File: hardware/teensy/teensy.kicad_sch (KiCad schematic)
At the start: 1 part, among them U1 Teensy3.5

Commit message: still learning kicad
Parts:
- added J1: CONN_16, Connectors:1X16, symbol SparkFun-Connectors:CONN_16
- added R1: 33OHM-0603-1_10W-1%, Resistors:AXIAL-0.3, symbol SparkFun-Resistors:33OHM-0603-1_10W-1%
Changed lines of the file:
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@@
     (stroke (width 0) (type solid) (color 0 0 0 0))
+  )
+  (symbol (lib_id "SparkFun-Resistors:33OHM-0603-1_10W-1%") (at 111.76 39.37 0) (unit 1)
+    (in_bom yes) (on_board yes)
+    (property "Reference" "R1" (id 0) (at 111.76 30.48 0)
+      (effects (font (size 1.143 1.143)))
+    )
+    (property "Value" "33OHM-0603-1_10W-1%" (id 1) (at 111.76 33.02 0)
+      (effects (font (size 1.143 1.143)))
+    )
+    (property "Footprint" "Resistors:AXIAL-0.3" (id 2) (at 111.76 35.56 0)
+      (effects (font (size 0.508 0.508)) hide)
+    )
+    (property "Datasheet" "" (id 3) (at 111.76 39.37 0)
+      (effects (font (size 1.524 1.524)) hide)
+    )
+    (property "Field4" "RES-08270" (id 4) (at 111.76 35.56 0)
+      (effects (font (size 1.524 1.524)))
+    )
+  )
+  (symbol (lib_id "SparkFun-Connectors:CONN_16") (at 68.58 68.58 0) (unit 1)
+    (in_bom yes) (on_board yes)
+    (property "Reference" "J1" (id 0) (at 67.31 22.86 0)
+      (effects (font (size 1.143 1.143)))
+    )
+    (property "Value" "CONN_16" (id 1) (at 67.31 25.4 0)
+      (effects (font (size 1.143 1.143)))
+    )
+    (property "Footprint" "Connectors:1X16" (id 2) (at 68.58 25.4 0)
+      (effects (font (size 0.508 0.508)) hide)
+    )
+    (property "Datasheet" "" (id 3) (at 68.58 68.58 0)
+      (effects (font (size 1.27 1.27)) hide)
+    )
+    (property "Field4" "XXX-00000" (id 4) (at 67.31 27.94 0)
+      (effects (font (size 1.524 1.524)))
+    )
   )
   (symbol (lib_id "teensy:Teensy3.5") (at 185.42 81.28 0) (unit 1)
@@
   )
   (symbol_instances
+    (path "/66d151a9-fc67-40c0-abf9-6a91841d98cd"
+      (reference "J1") (unit 1)
+    )
+    (path "/0dcce81d-b76c-41a1-a292-f1f972d63ccd"
+      (reference "R1") (unit 1)
+    )
     (path "/980fde8d-0f88-4d7e-9679-19d4aae9abd3"
       (reference "U1") (unit 1)

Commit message: added more to sch
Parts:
- added J2: CONN_16, Connectors:1X16, symbol SparkFun-Connectors:CONN_16
- added R10, R11, R12, R13, R14, R15, R16, R2, R3, R4, R5, R6, R7, R8, R9: 33OHM-0603-1_10W-1%, Resistors:AXIAL-0.3, symbol SparkFun-Resistors:33OHM-0603-1_10W-1%
- added R17, R18: 390KOHM-0603-1_10W-1%, Resistors:AXIAL-0.3, symbol SparkFun-Resistors:390KOHM-0603-1_10W-1%
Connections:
- net at R1.1: now also J1.10, J1.12, J1.14, J1.16, J1.2, J1.4, J1.6, J1.8, J2.10, J2.12, J2.14, J2.16, J2.2, J2.4, J2.6, J2.8, R10.1, R11.1, R12.1, R13.1, R14.1, R15.1, R16.1, R17.2, R18.1, R2.1, R3.1, R4.1, R5.1, R6.1, R7.1, R8.1, R9.1
- net ct16: now reaches R1.2
- net ct16: now also J1.15, U1.36 (39_A20)
- net ct9: now reaches J1.1
- net ct9: now also U1.43 (16_A2_SCL0_Touch), R12.2
- net ct14: now reaches J1.11
- net ct14: now also U1.34 (37_A18_PWM_SCL1), R2.2
- net ct15: now reaches J1.13
- net ct15: now also U1.35 (38_A19_PWM_SDA1), R9.2
- net ct10: now reaches J1.3
- net ct10: now also U1.23 (31_A12_RX4_CS1), R4.2
- net ct11: now reaches J1.5
- net ct11: now also U1.24 (32_A13_TX4_SCK1), R11.2
- net ct12: now reaches J1.7
- net ct12: now also U1.32 (35_A16_PWM), R3.2
- net ct13: now reaches J1.9
- net ct13: now also U1.33 (36_A17_PWM), R10.2
- net ct8: now reaches U1.30 (33_A14_TX5_CAN1TX_SCL0)
- net ct8: now also J2.15, R5.2
- net at U1.39 (GND): now also R18.2
- net ct1: now reaches U1.41 (14_A0_PWM_SCK0)
- net ct1: now also J2.1, R16.2
- net ct2: now reaches U1.42 (15_A1_CS0_Touch)
- net ct2: now also J2.3, R8.2
- net ct3: now reaches U1.44 (17_A3_SDA0_Touch)
- net ct3: now also J2.5, R15.2
- net ct4: now reaches U1.45 (18_A4_SDA0_Touch)
- net ct4: now also J2.7, R7.2
- net ct5: now reaches U1.46 (19_A5_SCL0_Touch)
- net ct5: now also J2.9, R14.2
- net ct6: now reaches U1.47 (20_A6_PWM_CS0_SCK1)
- net ct6: now also J2.11, R6.2
- net ct7: now reaches U1.50 (23_A9_PWM_Touch)
- net ct7: now also J2.13, R13.2
- net at U1.51 (3.3V): now also R17.1
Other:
- moved on the sheet: J1, R1, U1

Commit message: more wiring
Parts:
- removed R1, R10, R11, R12, R13, R14, R15, R16, R2, R3, R4, R5, R6, R7, R8, R9: 33OHM-0603-1_10W-1%, Resistors:AXIAL-0.3, symbol SparkFun-Resistors:33OHM-0603-1_10W-1%
- removed R17, R18: 390KOHM-0603-1_10W-1%, Resistors:AXIAL-0.3, symbol SparkFun-Resistors:390KOHM-0603-1_10W-1%
- added R1, R10, R11, R12, R13, R14, R15, R16, R17, R18, R2, R3, R4, R5, R6, R7, R8, R9: RESISTORAXIAL-0.3, Resistors:AXIAL-0.3, symbol SparkFun-Resistors:RESISTORAXIAL-0.3
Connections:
- net ct1: now also R16.P$2 (2)
- net ct10: now also R4.P$2 (2)
- net ct11: now also R11.P$2 (2)
- net ct12: now also R3.P$2 (2)
- net ct13: now also R10.P$2 (2)
- net ct14: now also R2.P$2 (2)
- net ct15: now also R9.P$2 (2)
- net ct16: now also R1.P$2 (2)
- net ct2: now also R8.P$2 (2)
- net ct3: now also R15.P$2 (2)
- net ct4: now also R7.P$2 (2)
- net ct5: now also R14.P$2 (2)
- net ct6: now also R6.P$2 (2)
- net ct7: now also R13.P$2 (2)
- net ct8: now also R5.P$2 (2)
- net ct9: now also R12.P$2 (2)
- net CT_BIAS: now reaches J1.10, J1.12, J1.14, J1.16, J1.2, J1.4, J1.6, J1.8, J2.10, J2.12, J2.14, J2.16, J2.2, J2.4, J2.6, J2.8
- net CT_BIAS: now also R1.P$1 (1), R10.P$1 (1), R11.P$1 (1), R12.P$1 (1), R13.P$1 (1), R14.P$1 (1), R15.P$1 (1), R16.P$1 (1), R17.P$2 (2), R18.P$1 (1), R2.P$1 (1), R3.P$1 (1), R4.P$1 (1), R5.P$1 (1), R6.P$1 (1), R7.P$1 (1), R8.P$1 (1), R9.P$1 (1)
- net 3.3V: now reaches U1.51 (3.3V)
- net 3.3V: now also R17.P$1 (1)
- net GND: now reaches U1.39 (GND)
- net GND: now also R18.P$2 (2)
- net at U1.2 (0_RX1_MOSI1_Touch): no longer U1.3 (1_TX1_MISO1_Touch)

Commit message: fully routed
ugly, but correct, i think.
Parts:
- added J3: CONN_04, Connectors:1X04, symbol SparkFun-Connectors:CONN_04
- added R19, R20, R21, R22: RESISTORAXIAL-0.3, Resistors:AXIAL-0.3, symbol SparkFun-Resistors:RESISTORAXIAL-0.3
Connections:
- net CT_BIAS: now also J3.2, J3.4, R20.P$2 (2), R21.P$1 (1)
- net ct10: now also U1.24 (32_A13_TX4_SCK1); no longer U1.23 (31_A12_RX4_CS1)
- net ct11: now also U1.32 (35_A16_PWM); no longer U1.24 (32_A13_TX4_SCK1)
- net ct12: now also U1.33 (36_A17_PWM); no longer U1.32 (35_A16_PWM)
- net ct13: now also U1.34 (37_A18_PWM_SCL1); no longer U1.33 (36_A17_PWM)
- net ct14: now also U1.35 (38_A19_PWM_SDA1); no longer U1.34 (37_A18_PWM_SCL1)
- net ct15: now also U1.36 (39_A20); no longer U1.35 (38_A19_PWM_SDA1)
- net ct16: now also U1.38 (A22_DAC1); no longer U1.36 (39_A20)
- net ct3: now also U1.43 (16_A2_SCL0_Touch); no longer U1.44 (17_A3_SDA0_Touch)
- net ct4: now also U1.44 (17_A3_SDA0_Touch); no longer U1.45 (18_A4_SDA0_Touch)
- net ct5: now also U1.45 (18_A4_SDA0_Touch); no longer U1.46 (19_A5_SCL0_Touch)
- net ct6: now also U1.46 (19_A5_SCL0_Touch); no longer U1.47 (20_A6_PWM_CS0_SCK1)
- net ct7: now also U1.47 (20_A6_PWM_CS0_SCK1); no longer U1.50 (23_A9_PWM_Touch)
- net ct8: now also U1.50 (23_A9_PWM_Touch); no longer U1.30 (33_A14_TX5_CAN1TX_SCL0)
- net ct9: now also U1.23 (31_A12_RX4_CS1); no longer U1.43 (16_A2_SCL0_Touch)
- net at U1.48 (21_A7_PWM_CS0_MOSI1): now also U1.57 (A11), R21.P$2 (2), R22.P$1 (1)
- net at U1.49 (22_A8_PWM_Touch): now also U1.56 (A10), R19.P$2 (2), R20.P$1 (1)
- new net L1: J3.1, R22.P$2 (2)
- new net L2: J3.3, R19.P$1 (1)
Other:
- moved on the sheet: J1, J2, R1, R10, R11, R12, R13, R14, R15, R16, R17, R18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

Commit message: good looking board now
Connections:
- net 3.3V: now also U1.15 (3.3V); no longer U1.51 (3.3V)
- net GND: now also U1.1 (GND); no longer U1.39 (GND)

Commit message: sch and pcb look good, also gbr and ngc outputs
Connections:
- net L2_SCALED: now reaches R19.P$2 (2), R20.P$1 (1), U1.49 (22_A8_PWM_Touch), U1.56 (A10)
- net L1_SCALED: now reaches R21.P$2 (2), R22.P$1 (1), U1.48 (21_A7_PWM_CS0_MOSI1), U1.57 (A11)

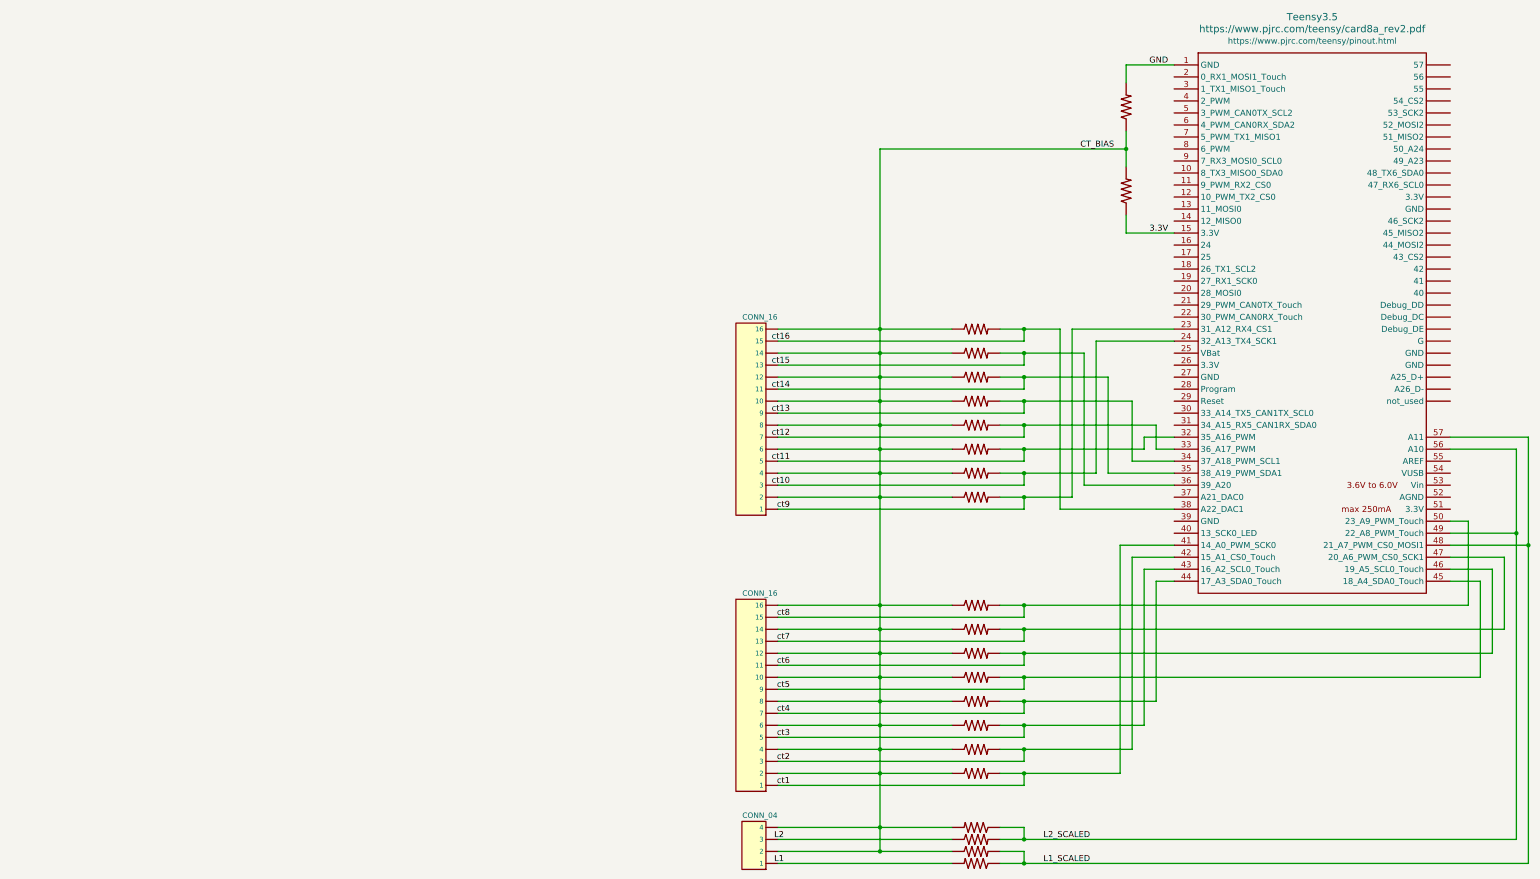
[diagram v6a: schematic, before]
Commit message: hoo boy, adc protection and bigger terminals
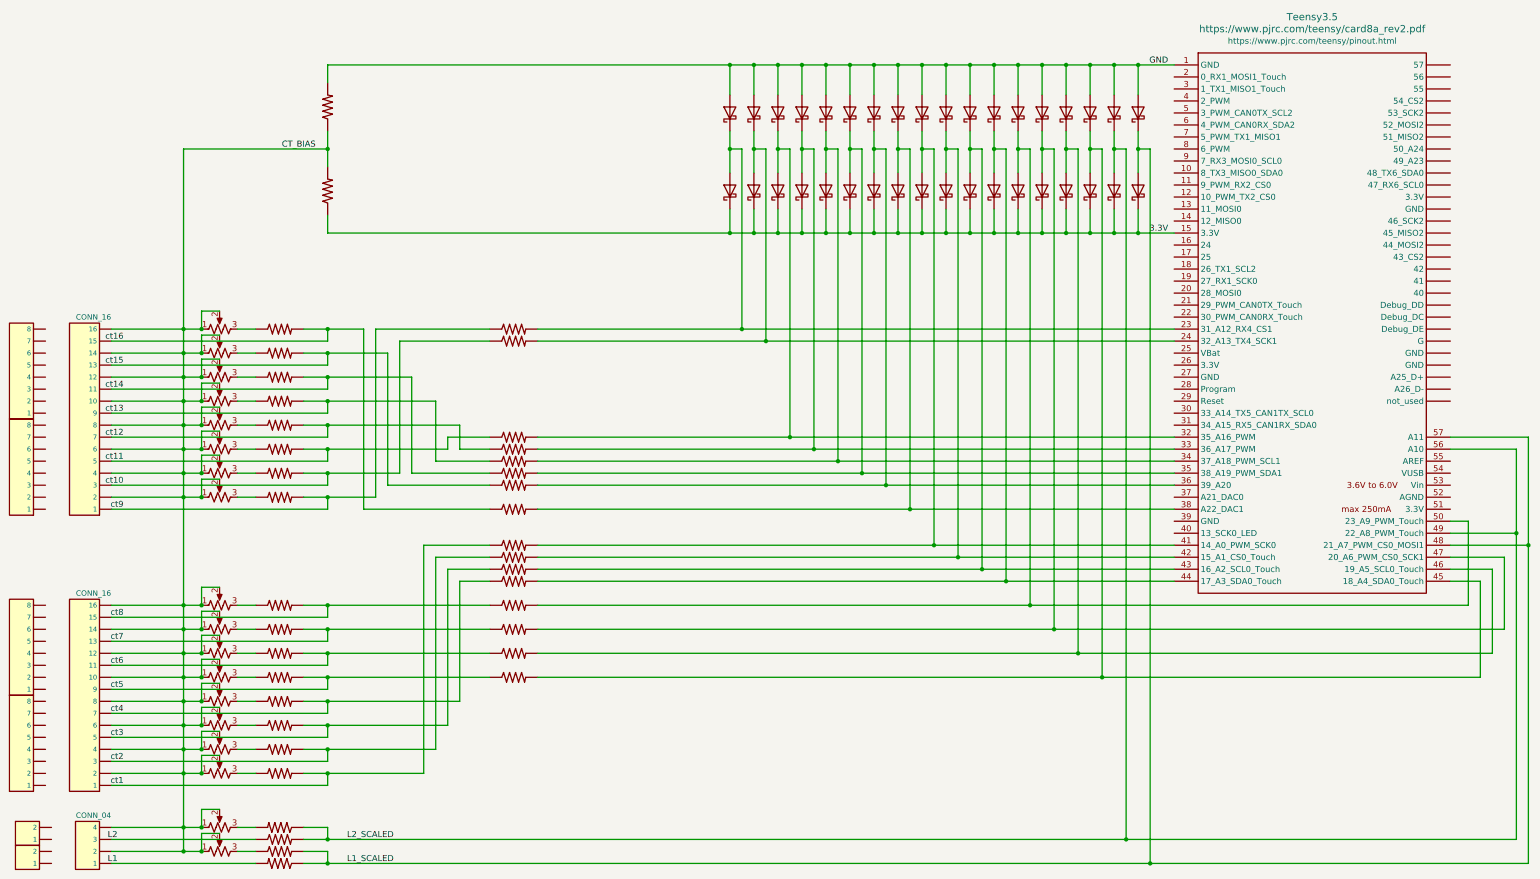
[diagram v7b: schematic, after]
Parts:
- added D1, D10, D11, D12, D13, D14, D15, D16, D17, D18, D19, D2, D20, D21, D22, D23, D24, D25, D26, D27, D28, D29, D3, D30, D31, D32, D33, D34, D35, D36, D4, D5, D6, D7, D8, D9: D_Schottky, Diode_SMD:D_SOD-123, symbol Device:D_Schottky
- added J4, J5, J6, J7: CONN_083.5MM-8, Connectors:SCREWTERMINAL-3.5MM-8, symbol SparkFun-Connectors:CONN_083.5MM-8
- added J8, J9: CONN_023.5MM, Connectors:SCREWTERMINAL-3.5MM-2, symbol SparkFun-Connectors:CONN_023.5MM
- added R23, R24, R25, R26, R27, R28, R29, R30, R31, R32, R33, R34, R35, R36, R37, R38: RESISTORAXIAL-0.3, Resistors:AXIAL-0.3, symbol SparkFun-Resistors:RESISTORAXIAL-0.3
- added RV1, RV10, RV11, RV12, RV13, RV14, RV15, RV16, RV17, RV18, RV2, RV3, RV4, RV5, RV6, RV7, RV8, RV9: R_POT_US, Potentiometer_THT:Potentiometer_Bourns_3296W_Vertical, symbol Device:R_POT_US
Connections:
- net 3.3V: now also D10.1 (K), D12.1 (K), D14.1 (K), D16.1 (K), D18.1 (K), D2.1 (K), D20.1 (K), D22.1 (K), D24.1 (K), D26.1 (K), D28.1 (K), D30.1 (K), D32.1 (K), D34.1 (K), D36.1 (K), D4.1 (K), D6.1 (K), D8.1 (K)
- net CT_BIAS: now also RV1.1, RV1.2, RV10.1, RV10.2, RV11.1, RV11.2, RV12.1, RV12.2, RV13.1, RV13.2, RV14.1, RV14.2, RV15.1, RV15.2, RV16.1, RV16.2, RV17.1, RV17.2, RV18.1, RV18.2, RV2.1, RV2.2, RV3.1, RV3.2, RV4.1, RV4.2, RV5.1, RV5.2, RV6.1, RV6.2, RV7.1, RV7.2, RV8.1, RV8.2, RV9.1, RV9.2; no longer R1.P$1 (1), R10.P$1 (1), R11.P$1 (1), R12.P$1 (1), R13.P$1 (1), R14.P$1 (1), R15.P$1 (1), R16.P$1 (1), R2.P$1 (1), R20.P$2 (2), R21.P$1 (1), R3.P$1 (1), R4.P$1 (1), R5.P$1 (1), R6.P$1 (1), R7.P$1 (1), R8.P$1 (1), R9.P$1 (1)
- net GND: now also D1.2 (A), D11.2 (A), D13.2 (A), D15.2 (A), D17.2 (A), D19.2 (A), D21.2 (A), D23.2 (A), D25.2 (A), D27.2 (A), D29.2 (A), D3.2 (A), D31.2 (A), D33.2 (A), D35.2 (A), D5.2 (A), D7.2 (A), D9.2 (A)
- net L1_SCALED: now also D35.1 (K), D36.2 (A)
- net L2_SCALED: now also D33.1 (K), D34.2 (A)
- net ct1: now also R31.P$1 (1); no longer U1.41 (14_A0_PWM_SCK0)
- net ct10: now also R24.P$1 (1); no longer U1.24 (32_A13_TX4_SCK1)
- net ct11: now also R25.P$1 (1); no longer U1.32 (35_A16_PWM)
- net ct12: now also R26.P$1 (1); no longer U1.33 (36_A17_PWM)
- net ct13: now also R27.P$1 (1); no longer U1.34 (37_A18_PWM_SCL1)
- net ct14: now also R28.P$1 (1); no longer U1.35 (38_A19_PWM_SDA1)
- net ct15: now also R29.P$1 (1); no longer U1.36 (39_A20)
- net ct16: now also R30.P$1 (1); no longer U1.38 (A22_DAC1)
- net ct2: now also R32.P$1 (1); no longer U1.42 (15_A1_CS0_Touch)
- net ct3: now also R33.P$1 (1); no longer U1.43 (16_A2_SCL0_Touch)
- net ct4: now also R34.P$1 (1); no longer U1.44 (17_A3_SDA0_Touch)
- net ct5: now also R38.P$1 (1); no longer U1.45 (18_A4_SDA0_Touch)
- net ct6: now also R37.P$1 (1); no longer U1.46 (19_A5_SCL0_Touch)
- net ct7: now also R36.P$1 (1); no longer U1.47 (20_A6_PWM_CS0_SCK1)
- net ct8: now also R35.P$1 (1); no longer U1.50 (23_A9_PWM_Touch)
- net ct9: now also R23.P$1 (1); no longer U1.23 (31_A12_RX4_CS1)
- new net: R9.P$1 (1), RV2.3
- new net: D25.1 (K), D26.2 (A), R35.P$2 (2), U1.50 (23_A9_PWM_Touch)
- new net: R3.P$1 (1), RV5.3
- new net: R10.P$1 (1), RV4.3
- new net: D3.1 (K), D4.2 (A), R24.P$2 (2), U1.24 (32_A13_TX4_SCK1)
- new net: R12.P$1 (1), RV8.3
- new net: R6.P$1 (1), RV11.3
- new net: R20.P$2 (2), RV17.3
- new net: D10.2 (A), D9.1 (K), R27.P$2 (2), U1.34 (37_A18_PWM_SCL1)
- new net: R8.P$1 (1), RV15.3
- new net: D19.1 (K), D20.2 (A), R32.P$2 (2), U1.42 (15_A1_CS0_Touch)
- new net: D27.1 (K), D28.2 (A), R36.P$2 (2), U1.47 (20_A6_PWM_CS0_SCK1)
- new net: R16.P$1 (1), RV16.3
- new net: D31.1 (K), D32.2 (A), R38.P$2 (2), U1.45 (18_A4_SDA0_Touch)
- new net: R7.P$1 (1), RV13.3
- new net: R11.P$1 (1), RV6.3
- new net: R4.P$1 (1), RV7.3
- new net: R15.P$1 (1), RV14.3
- new net: D15.1 (K), D16.2 (A), R30.P$2 (2), U1.38 (A22_DAC1)
- new net: D29.1 (K), D30.2 (A), R37.P$2 (2), U1.46 (19_A5_SCL0_Touch)
- new net: D21.1 (K), D22.2 (A), R33.P$2 (2), U1.43 (16_A2_SCL0_Touch)
- new net: R14.P$1 (1), RV12.3
- new net: R21.P$1 (1), RV18.3
- new net: R1.P$1 (1), RV1.3
- new net: D5.1 (K), D6.2 (A), R25.P$2 (2), U1.32 (35_A16_PWM)
- new net: R13.P$1 (1), RV10.3
- new net: D11.1 (K), D12.2 (A), R28.P$2 (2), U1.35 (38_A19_PWM_SDA1)
- new net: D23.1 (K), D24.2 (A), R34.P$2 (2), U1.44 (17_A3_SDA0_Touch)
- new net: D13.1 (K), D14.2 (A), R29.P$2 (2), U1.36 (39_A20)
- new net: D1.1 (K), D2.2 (A), R23.P$2 (2), U1.23 (31_A12_RX4_CS1)
- new net: D7.1 (K), D8.2 (A), R26.P$2 (2), U1.33 (36_A17_PWM)
- new net: D17.1 (K), D18.2 (A), R31.P$2 (2), U1.41 (14_A0_PWM_SCK0)
- new net: R5.P$1 (1), RV9.3
- new net: R2.P$1 (1), RV3.3

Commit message: layout
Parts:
- removed J1, J2: CONN_16, Connectors:1X16, symbol SparkFun-Connectors:CONN_16
- removed J3: CONN_04, Connectors:1X04, symbol SparkFun-Connectors:CONN_04
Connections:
- net CT_BIAS: now also J4.2, J4.4, J4.6, J4.8, J5.2, J5.4, J5.6, J5.8, J6.2, J6.4, J6.6, J6.8, J7.2, J7.4, J7.6, J7.8, J8.2, J9.2
- net L1: now also J9.1
- net L2: now also J8.1
- net ct1: now also J7.1
- net ct10: now also J5.3
- net ct11: now also J5.5
- net ct12: now also J5.7
- net ct13: now also J4.1
- net ct14: now also J4.3
- net ct15: now also J4.5
- net ct16: now also J4.7
- net ct2: now also J7.3
- net ct3: now also J7.5
- net ct4: now also J7.7
- net ct5: now also J6.1
- net ct6: now also J6.3
- net ct7: now also J6.5
- net ct8: now also J6.7
- net ct9: now also J5.1
